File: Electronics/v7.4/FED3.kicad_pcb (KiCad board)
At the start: 4 copper layers, 108 x 50 mm, 91 parts, among them IC1 MC74VHC1GT125, IC2 TB6612FNG, IC4 RTC PCF8523T, J1 Conn_02x03_Odd_Even, Q2 DMP2035U-7, SW1 Sw, SW2 SPST_TACT-KMR2, U1 ATSAMD21G18A, U2 MIC5504-3.3, U3 MCP73831T, X1 ClockXtal, X2 uXtal, X4 microsd, X5 JST-XH-02

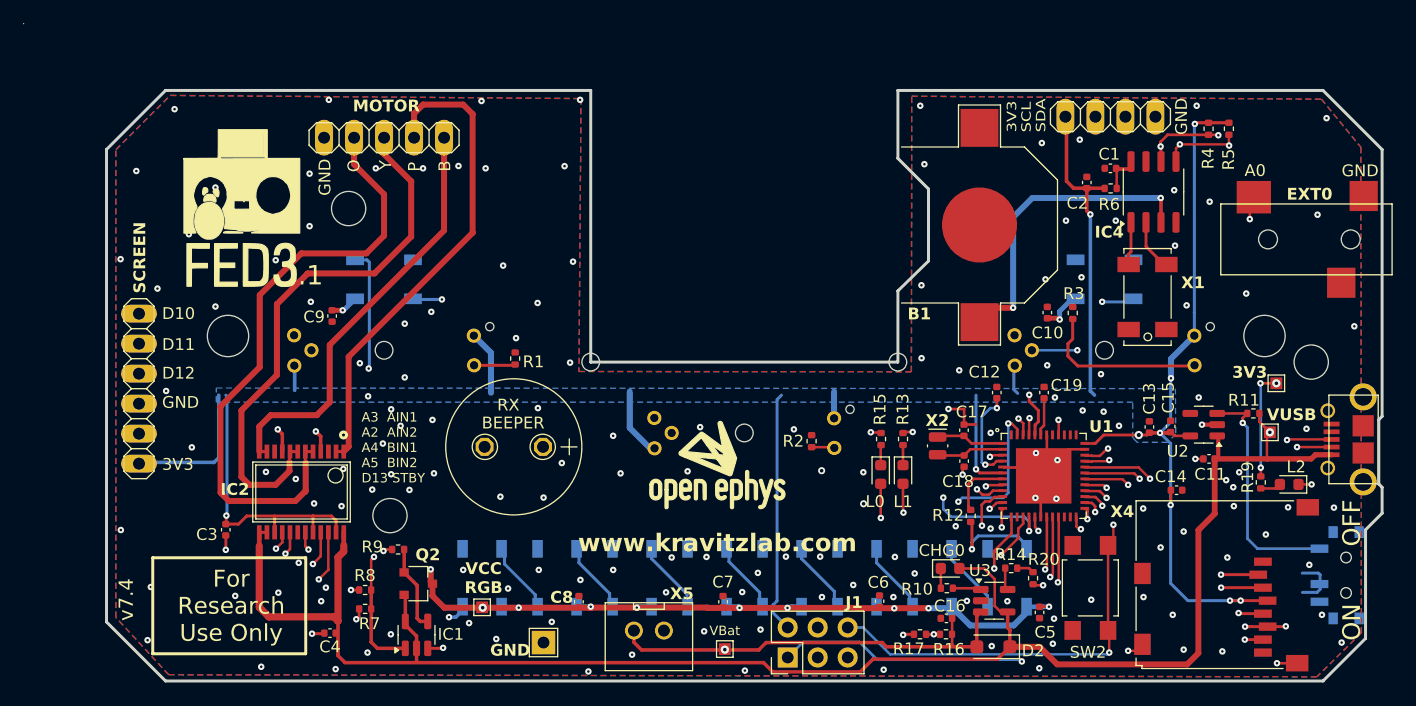
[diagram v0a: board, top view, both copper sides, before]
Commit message: Decreased consumption and added STEMMA connector.
- Updated Bat's resistor divider to 0.1% tolerance
- Reduced LEDs' current to bellow 1 mA
- Updated buzzer model
- Increased available voltage to motor
- Added STEMMA (2mm ) connector

To do:
- Update STEMMA to STEMMA QT (2mm)
- (Maybe) Update charging current to slightly bellow 500 mA

Co-Authored-By: David Palma <78764277+davidpalma666@users.noreply.github.com>
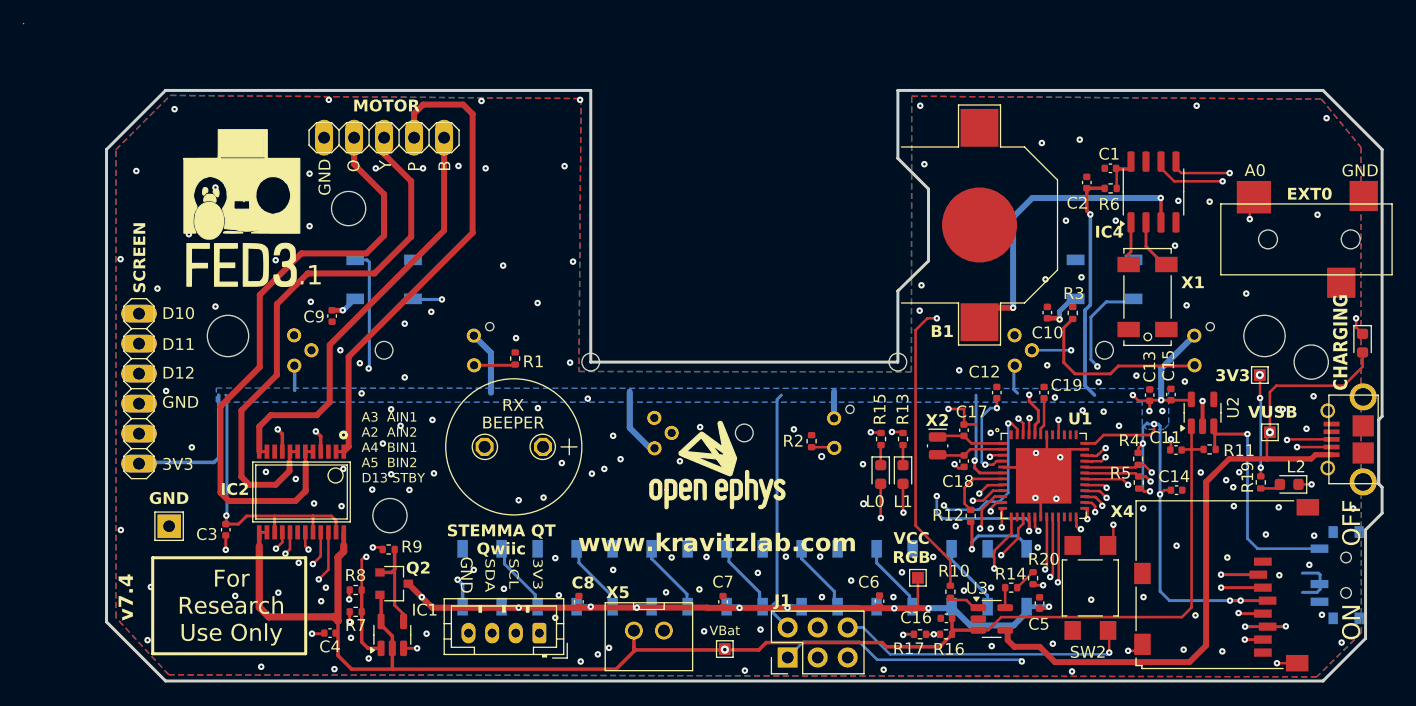
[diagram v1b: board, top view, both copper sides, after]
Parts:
- removed @HOLE4: , 
- removed D2: SM5817PL, Diode_SMD:D_SOD-123F
- added ?: , , F.Cu at (212.6, 100.5)
- AUX_I2C0: footprint FED3_PCBLib:1X04 -> Connector_JST:JST_PH_B4B-PH-K_1x04_P2.00mm_Vertical
- G***: footprint FED3.1 v7.4:oe logo -> FED3_PCBLib:oe logo
- L2: value RED -> DNP
- R11, R16, R17: value 100k -> 100k 0.1%
- R13: value 68R -> 2k2
- R15: value 68R -> 10k
- R19: value 68R -> DNP
- moved AUX_I2C0 65.2 mm to (131.2, 126.0), turned to 180 degrees
- moved CHG0 39.8 mm to (200.8, 101.4), turned to -90 degrees
- moved TP2 37.0 mm to (163.2, 121.3)
- moved TP5 33.2 mm to (99.8, 116.9)
- moved R5 30.9 mm to (181.9, 113.2), turned to -90 degrees
- moved R4 28.6 mm to (181.8, 111.2)
- moved R11 4.80 mm to (187.9, 110.4), turned to 0 degrees
- moved C11 2.90 mm to (185.1, 110.5)
- moved C13 2.70 mm to (182.8, 105.8)
- moved C15 2.70 mm to (184.6, 105.8)
- moved Q2 2.05 mm to (118.8, 121.8)
- moved IC1 2.05 mm to (118.7, 126.1)
- moved R14 1.65 mm to (171.1, 122.1)
- moved TP1 1.57 mm to (192.2, 104.1)
- moved U3 1.56 mm to (169.4, 124.8)
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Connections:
- net D7 renamed /controler stage/D7
- C11 pad 1: VUSB -> VBat
- C4 pad 1: VUSB -> VBat
- IC1 pad 2: VUSB -> VBat
- IC1 pad 5: VUSB -> VBat
- IC2 pad 13: VUSB -> VBat
- IC2 pad 14: VUSB -> VBat
- IC2 pad 24: VUSB -> VBat
- Q2 pad P$2: VUSB -> VBat
- R11 pad 1: VUSB -> VBat
- U2 pad 1: VUSB -> VBat
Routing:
- net VUSB: track 149.2 -> 60.3 mm
- net VBat: track 37.5 -> 126.3 mm
- net /controler stage/SDA: track 54.1 -> 117.7 mm, vias 4 -> 5
- net Net-(CHG0-K): track 1.67 -> 62.8 mm, vias 0 -> 2
- net /controler stage/SCL: track 55.4 -> 114.9 mm, vias 4 -> 5
- net +3V3: track 228.6 -> 236.0 mm, vias 18 -> 22
- net /IOs Interface/VCCNEO: track 124.8 -> 130.7 mm, vias 12 -> 11
- net /controler stage/~{RESET}: track 48.7 -> 52.4 mm
- net Net-(LED8-DO): track 31.0 -> 29.5 mm
- net A2: track 68.8 -> 70.2 mm
- net Net-(PI1-Pad2): track 14.3 -> 15.7 mm
- net GND: track 37.2 -> 38.5 mm, vias 157 -> 160
- net D13: track 85.2 -> 84.0 mm
- net Net-(IC1-P$4): track 7.29 -> 7.91 mm
- net /controler stage/D10: track 96.4 -> 97.0 mm
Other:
- board text added: "CHARGING"
- board text added: "Qwiic"
- board text added: "STEMMA QT"

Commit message: Updated supply circuit, battery charge current, and added a new connector.
- Added a STEMMA QT / Qwiic connector for expansion.
- Made the entire supply being sourced from the battery.
- Reduced battery charging to 455 mA (previously was 500 mA).

Co-Authored-By: David Palma <78764277+davidpalma666@users.noreply.github.com>
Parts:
- removed R20: 1k, Resistor_SMD:R_0402_1005Metric
- AUX_I2C0: value DNP -> Qwiic; footprint Connector_JST:JST_PH_B4B-PH-K_1x04_P2.00mm_Vertical -> Connector_JST:JST_SH_BM04B-SRSS-TB_1x04-1MP_P1.00mm_Vertical
- R14: value 1k -> 2k2
- moved AUX_I2C0 3.17 mm to (128.0, 126.3)
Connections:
- AUX_I2C0 pad 1: +3V3 -> GND
- AUX_I2C0 pad 2: /controler stage/SCL -> +3V3
- AUX_I2C0 pad 4: GND -> /controler stage/SCL
- R14 pad 1: Net-(R14-Pad1) -> GND
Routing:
- net +3V3: track 236.0 -> 240.3 mm, vias 22 -> 23
- net /controler stage/SCL: track 114.9 -> 118.1 mm, vias 5 -> 6
- net Net-(R14-Pad1): track 1.88 -> 0.00 mm
- net /controler stage/SDA: track 117.7 -> 119.3 mm, vias 5 -> 6
- net GND: track 38.5 -> 39.6 mm
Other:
- board text added: ".2"
- board text removed: ".1"

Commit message: Prepared files for production.
Also fixed #13
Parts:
- moved ? 20.0 mm to (192.5, 100.8)
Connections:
- net /controler stage/AREF renamed /Controller Stage/AREF
- net /controler stage/D10 renamed /Controller Stage/D10
- net /controler stage/D11 renamed /Controller Stage/D11
- net /controler stage/D12 renamed /Controller Stage/D12
- net /controler stage/D7 renamed /Controller Stage/D7
- net /controler stage/MISO renamed /Controller Stage/MISO
- net /controler stage/MOSI renamed /Controller Stage/MOSI
- net /controler stage/SCK renamed /Controller Stage/SCK
- net /controler stage/SCL renamed /Controller Stage/SCL
- net /controler stage/SDA renamed /Controller Stage/SDA
- net /controler stage/SD_CS renamed /Controller Stage/SD_CS
- net /controler stage/SQW renamed /Controller Stage/SQW
- net /controler stage/SWCLK renamed /Controller Stage/SWCLK
- net /controler stage/SWDIO renamed /Controller Stage/SWDIO
- net /controler stage/~{RESET} renamed /Controller Stage/~{RESET}
